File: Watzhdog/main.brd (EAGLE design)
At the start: 100 x 80 mm, 44 parts, among them CN1 MICROUSB(MC-5F-02), IC1 C8051F381-GM, IC3 N25Q512A, IC6 MPU-9250, U1 MCP73831, U2 TPS61201

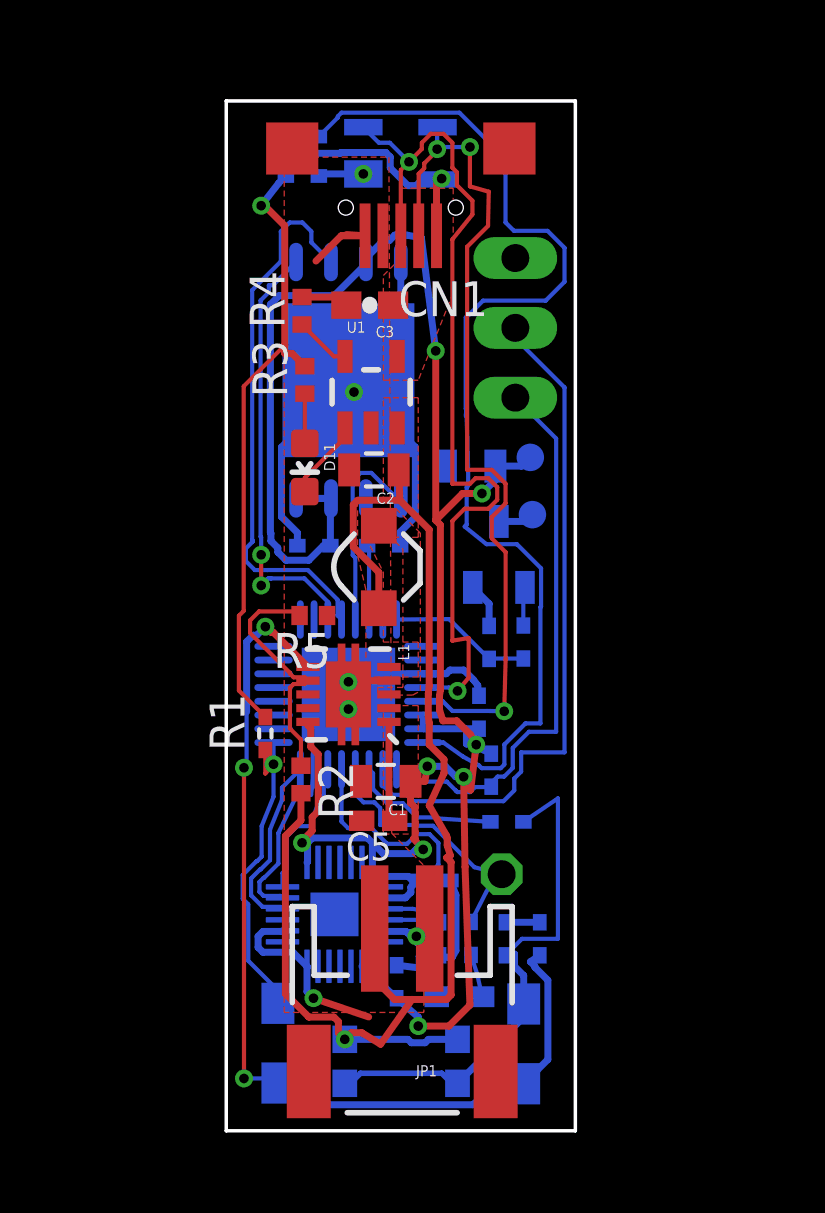
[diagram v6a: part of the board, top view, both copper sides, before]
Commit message: Modified circuit shape
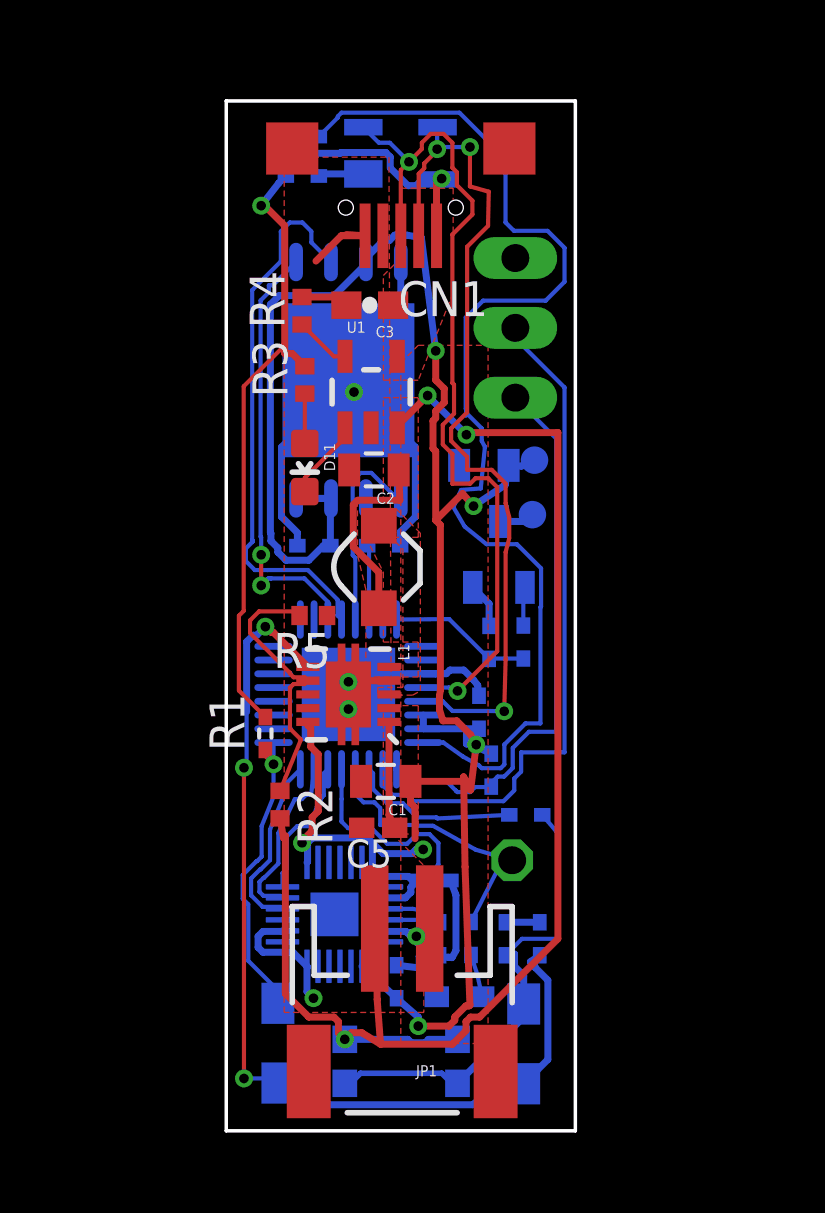
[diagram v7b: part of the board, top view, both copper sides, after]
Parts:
- moved R2 1.19 mm to (52.8, 38.5)
- moved R16 0.73 mm to (61.7, 38.2)
- moved JP2 0.64 mm to (61.2, 36.5)
- moved C6 0.48 mm to (60.2, 50.9)
- moved C5 0.25 mm to (56.3, 37.7)
- moved MP 0.18 mm to (62.0, 51.1)
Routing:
- net VBAT: track 49.5 -> 60.3 mm, vias 1 -> 3
- net DGND: track 59.0 -> 56.9 mm, vias 6 -> 5
- net N$11: track 19.4 -> 17.4 mm
- net UVLO: track 9.06 -> 10.1 mm
- net N$18: track 40.7 -> 41.7 mm
- net D+: track 32.8 -> 31.8 mm
- net N$5: track 5.50 -> 6.18 mm
- net N$7: track 11.7 -> 11.0 mm
- net VCC: track 86.6 -> 86.2 mm, vias 8 -> 6
